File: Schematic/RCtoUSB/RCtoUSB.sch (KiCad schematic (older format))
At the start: 21 parts, among them J1 Power, J2 PORTA, J3 SAT, J4 ICSP, J5 PORTB, J6 USB_B_Mini, Q1 2N7002P_215, U1 AP2210N-3.3TRG1, U2 PIC18f27J53

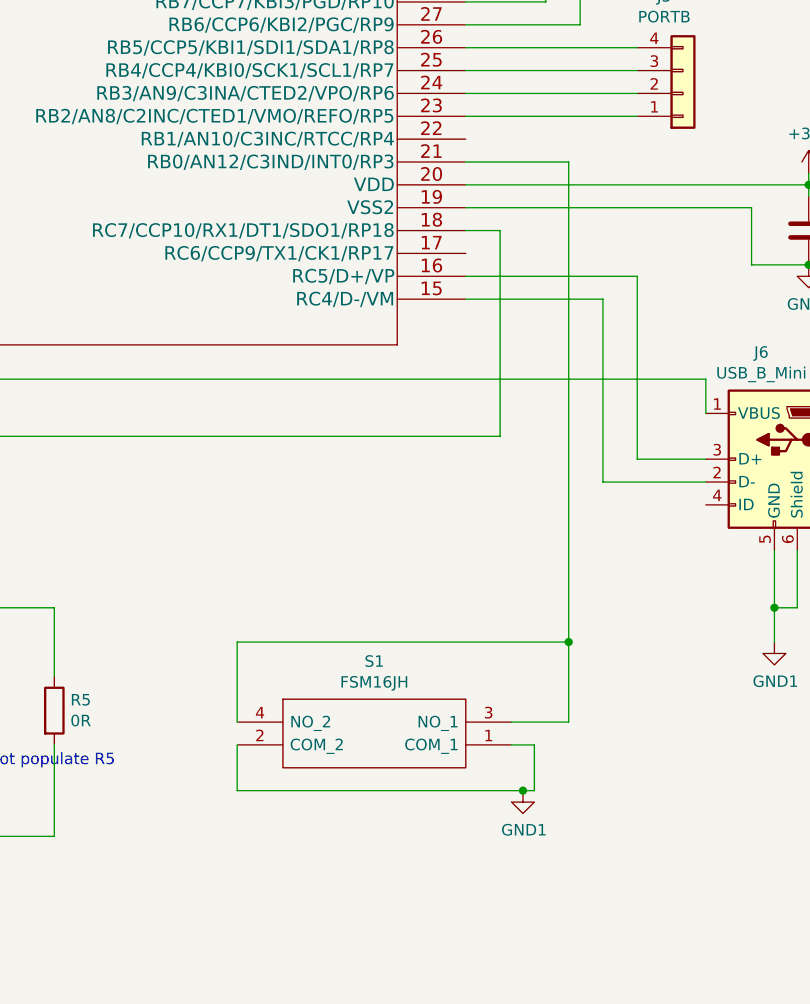
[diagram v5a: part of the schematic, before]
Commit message: Improved switch symbol in schematic
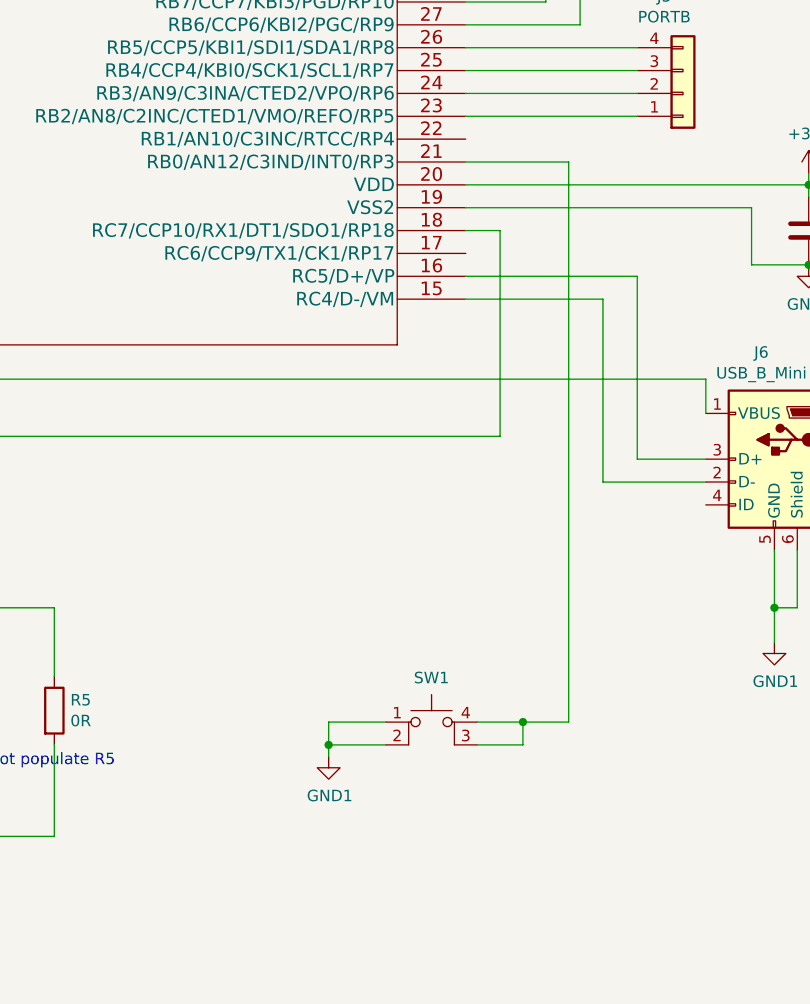
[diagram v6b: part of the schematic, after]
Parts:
- removed S1: FSM16JH, SamacSys_Parts:FSM16JH, symbol SamacSys_Parts:FSM16JH
- added SW1: SW_MEC_5E, SamacSys_Parts:FSM16JH, symbol Switch:SW_MEC_5E
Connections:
- net GND1: now also SW1.1, SW1.2
- net at U2.21 (RB0/AN12/C3IND/INT0/RP3): now also SW1.3 (K), SW1.4 (A)
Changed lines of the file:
@@
 L power:GND1 #PWR012
 U 1 1 60FC2FDD
-P 8350 6050
-F 0 "#PWR012" H 8350 5800 50  0001 C CNN
-F 1 "GND1" H 8355 5877 50  0000 C CNN
-F 2 "" H 8350 6050 50  0001 C CNN
-F 3 "" H 8350 6050 50  0001 C CNN
-	1    8350 6050
+P 7500 5900
+F 0 "#PWR012" H 7500 5650 50  0001 C CNN
+F 1 "GND1" H 7505 5727 50  0000 C CNN
+F 2 "" H 7500 5900 50  0001 C CNN
+F 3 "" H 7500 5900 50  0001 C CNN
+	1    7500 5900
 	1    0    0    -1
 $EndComp
@@
 $EndComp
 $Comp
-L SamacSys_Parts:FSM16JH S1
-U 1 1 60FB5582
-P 7100 5750
-F 0 "S1" H 7700 6015 50  0000 C CNN
-F 1 "FSM16JH" H 7700 5924 50  0000 C CNN
-F 2 "SamacSys_Parts:FSM16JH" H 8150 5850 50  0001 L CNN
-F 3 "https://www.te.com/commerce/DocumentDelivery/DDEController?Action=showdoc&DocId=Customer+Drawing%7F1825910%7FC10%7Fpdf%7FEnglish%7FENG_CD_1825910_C10.pdf%7F3-1825910-1" H 8150 5750 50  0001 L CNN
-F 4 "Tactile Switches 6MM TACT SWITCH" H 8150 5650 50  0001 L CNN "Description"
-F 5 "17.3" H 8150 5550 50  0001 L CNN "Height"
-F 6 "506-FSM16JH" H 8150 5450 50  0001 L CNN "Mouser Part Number"
-F 7 "https://www.mouser.co.uk/ProductDetail/TE-Connectivity-PB/FSM16JH/?qs=eA0sQYb2Mifk48vugSh4aw%3D%3D" H 8150 5350 50  0001 L CNN "Mouser Price/Stock"
-F 8 "TE Connectivity" H 8150 5250 50  0001 L CNN "Manufacturer_Name"
-F 9 "FSM16JH" H 8150 5150 50  0001 L CNN "Manufacturer_Part_Number"
-	1    7100 5750
-	1    0    0    -1
-$EndComp
-$Comp
 L Device:R R4
 U 1 1 60FB794B
@@
 	9550 5250 9450 5250
 Wire Wire Line
-	8550 5750 8300 5750
-Wire Wire Line
-	8300 5850 8400 5850
-Wire Wire Line
-	8400 5850 8400 6050
-Wire Wire Line
-	8400 6050 8350 6050
-Wire Wire Line
-	7100 5750 7100 5400
-Wire Wire Line
-	7100 5400 8550 5400
-Connection ~ 8550 5400
-Wire Wire Line
-	8550 5400 8550 5750
-Wire Wire Line
-	7100 6050 8350 6050
-Wire Wire Line
-	7100 5850 7100 6050
-Connection ~ 8350 6050
-Wire Wire Line
 	3450 3700 3000 3700
 Wire Wire Line
@@
 Wire Wire Line
 	6300 6250 5350 6250
-Wire Wire Line
-	8550 3300 8550 5400
 Wire Wire Line
 	8100 3300 8550 3300
@@
 Text Notes 5900 5950 0    50   ~ 0
 Do not populate R5
+$Comp
+L Switch:SW_MEC_5E SW1
+U 1 1 616B412F
+P 7950 5850
+F 0 "SW1" H 7950 6143 50  0000 C CNN
+F 1 "SW_MEC_5E" H 7950 6144 50  0001 C CNN
+F 2 "SamacSys_Parts:FSM16JH" H 7950 6150 50  0001 C CNN
+F 3 "http://www.apem.com/int/index.php?controller=attachment&id_attachment=1371" H 7950 6150 50  0001 C CNN
+	1    7950 5850
+	1    0    0    -1
+$EndComp
+Wire Wire Line
+	8550 3300 8550 5750
+Wire Wire Line
+	8150 5750 8350 5750
+Wire Wire Line
+	8150 5850 8350 5850
+Wire Wire Line
+	8350 5850 8350 5750
+Connection ~ 8350 5750
+Wire Wire Line
+	8350 5750 8550 5750
+Wire Wire Line
+	7750 5850 7500 5850
+Wire Wire Line
+	7500 5850 7500 5900
+Wire Wire Line
+	7750 5750 7500 5750
+Wire Wire Line
+	7500 5750 7500 5850
+Connection ~ 7500 5850
 $EndSCHEMATC
